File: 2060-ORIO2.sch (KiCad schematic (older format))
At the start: 197 parts, among them J11 RaspberryPI-B+header, J12 Conn_01x04, J13 Conn_01x08, J14 Conn_01x02, J15 Conn_01x08, J16 Conn_01x10, J17 Conn_01x10, J18 Conn_01x10, J19 Conn_01x10, J20 Conn_01x09, J21 Conn_01x08, J22 Conn_01x08, J23 Conn_01x08, J24 Conn_01x08, J25 Conn_01x08, J26 Conn_01x08, J28 Conn_01x16, J29 Conn_01x16, J30 Conn_01x16, J31 Conn_01x08, J32 Conn_01x08, J33 Conn_01x08, J34 Conn_01x08, J35 TBL001-500-02GY-2GY, Q11 ULN2803ADWR, Q12 BCV27, Q91 BCV27, Q92 BCV27, Q93 BCV27, Q94 BCV27, SW1 SW_DIP_x01, SW11 SW_DIP_x08, U1 AOZ2151TQI-19, U11 ICE40HX4K-TQ144, U12 ‎74LVT245B, U13 ‎74LVT245B, U14 ‎74LVT245B, U15 AOZ2151TQI-19, U16 MCP3008, U17 AZ1117CH-3.3TRG1, U18 AZ1117CH-3.3TRG1, U19 AZ1117CH-1.2, U20 AOZ2151TQI-19, U21 ‎74LVT245B, U22 ‎74LVT245B, U23 ‎74LVT245B, U24 ‎74LVT245B, U26 AP3012, Y11 XLH536025_000000I

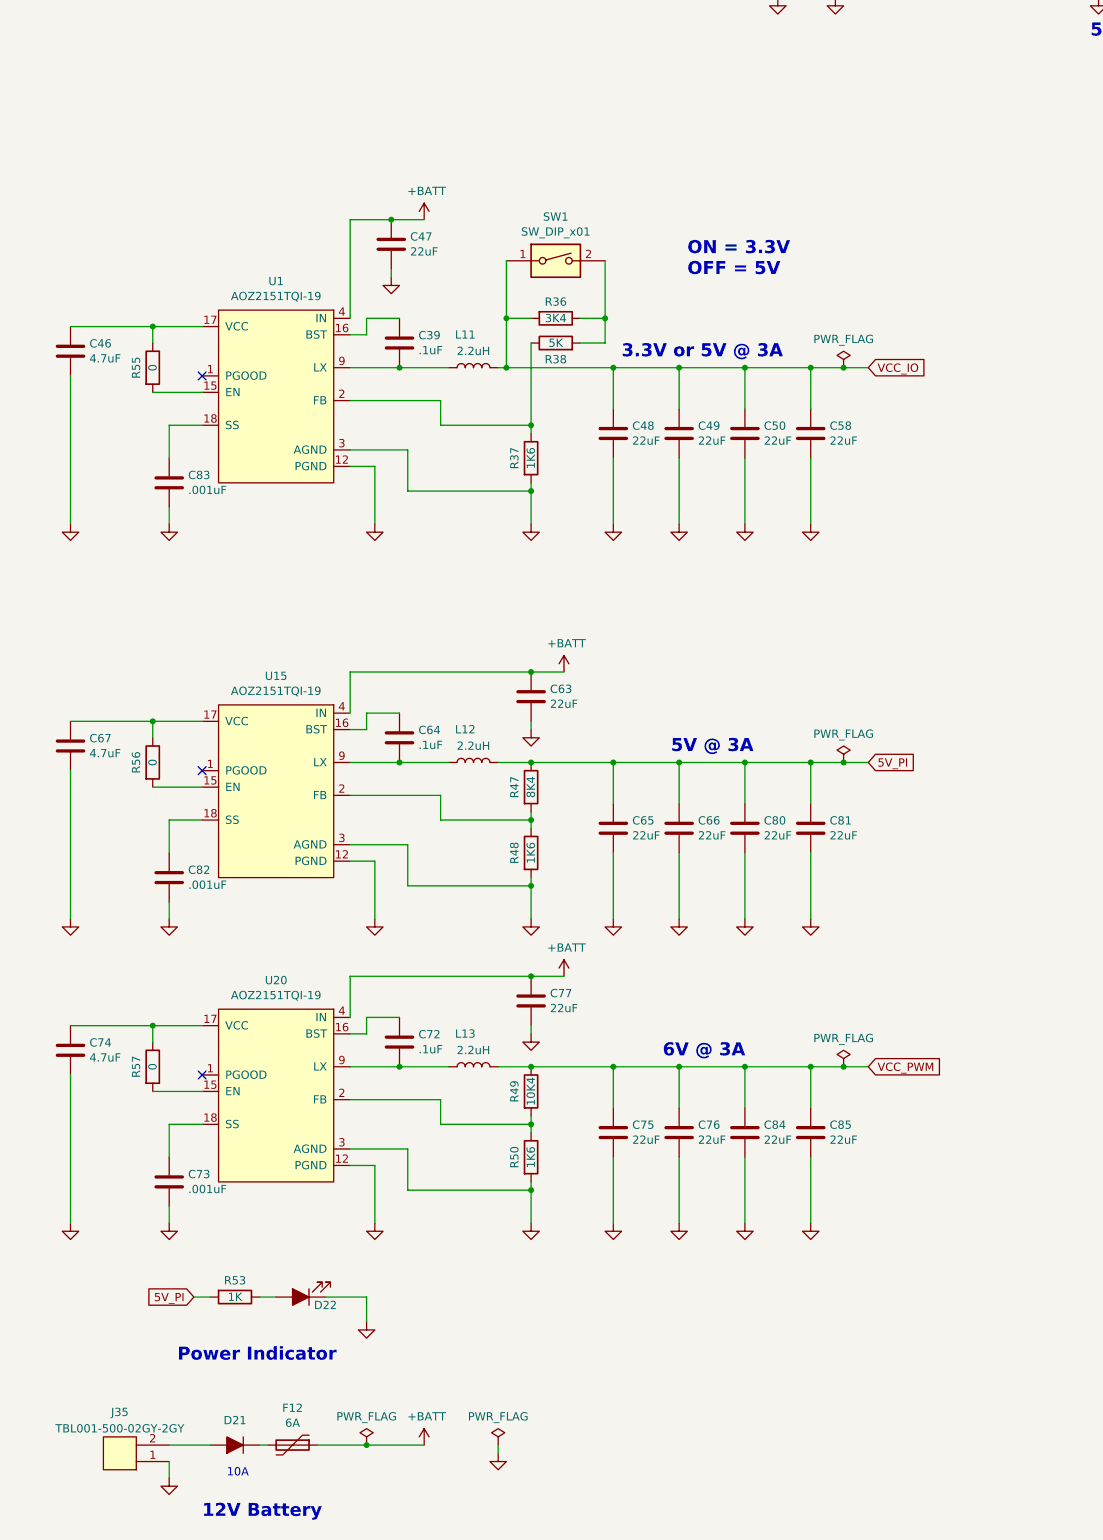
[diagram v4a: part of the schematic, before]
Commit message: Replace AOZ2151TQI-19 regulators with AP63300WU-7
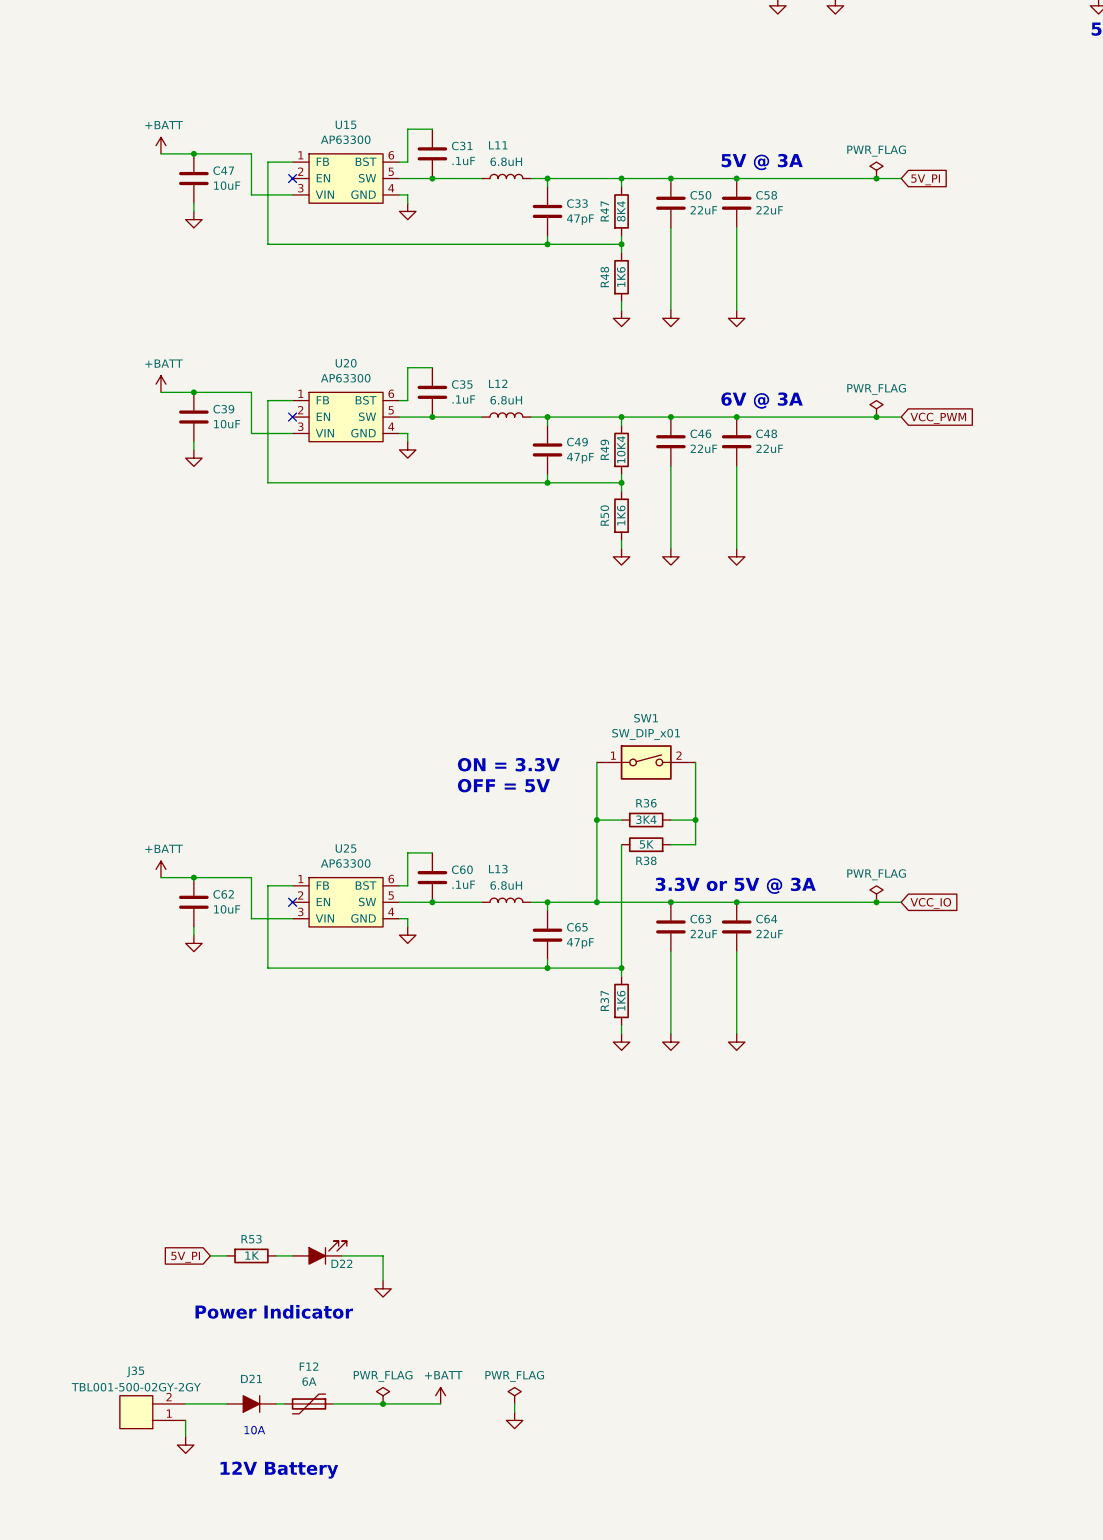
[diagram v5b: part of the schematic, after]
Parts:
- removed C66, C75, C76, C77, C80, C81, C84, C85: 22uF, Capacitor_SMD:C_0805_2012Metric_Pad1.15x1.40mm_HandSolder, symbol Device:C
- removed C67, C74: 4.7uF, Capacitor_SMD:C_0603_1608Metric_Pad1.05x0.95mm_HandSolder, symbol Device:C
- removed C72: .1uF, Capacitor_SMD:C_0603_1608Metric_Pad1.05x0.95mm_HandSolder, symbol Device:C
- removed C73, C82, C83: .001uF, Capacitor_SMD:C_0603_1608Metric_Pad1.05x0.95mm_HandSolder, symbol Device:C
- removed R55, R56, R57: 0, Resistor_SMD:R_0603_1608Metric_Pad1.05x0.95mm_HandSolder, symbol Device:R
- removed U1, U15, U20: AOZ2151TQI-19, jb-footprint:AOZ2151TQI-19, symbol jb-symbol:AOZ2151TQI-19
- added C31, C35, C60: .1uF, Capacitor_SMD:C_0603_1608Metric_Pad1.05x0.95mm_HandSolder, symbol Device:C
- added C33: 47pF, Capacitor_SMD:C_0603_1608Metric_Pad1.05x0.95mm_HandSolder, symbol Device:C
- added C62: 10uF, Capacitor_SMD:C_0805_2012Metric_Pad1.15x1.40mm_HandSolder, symbol Device:C
- added U15, U20, U25: AP63300, Package_TO_SOT_SMD:SOT-23-6, symbol jb-symbol:AP63300
- C39: value .1uF -> 10uF; footprint Capacitor_SMD:C_0603_1608Metric_Pad1.05x0.95mm_HandSolder -> Capacitor_SMD:C_0805_2012Metric_Pad1.15x1.40mm_HandSolder; Description CAP CER 0.1UF 25V X5R 0603 -> (none); Digi-Key_PN 445-6854-1-ND -> (none); MPN C1608X5R1E104K -> (none); Manufacturer TDK Corporation -> (none)
- C46: value 4.7uF -> 22uF; footprint Capacitor_SMD:C_0603_1608Metric_Pad1.05x0.95mm_HandSolder -> Capacitor_SMD:C_0805_2012Metric_Pad1.15x1.40mm_HandSolder; Description CAP CER 4.7UF 10V X5R 0603 -> CAP CER 22UF 10V X5R 0805; Digi-Key_PN 1276-1044-1-ND -> 490-10746-1-ND; MPN CL10A475KP8NNNC -> GRM21BR61A226ME44L; Manufacturer Samsung Electro-Mechanics -> Murata Electronics
- C47: value 22uF -> 10uF; Description CAP CER 22UF 25V X5R 0805 -> (none); Digi-Key_PN 490-14661-1-ND -> (none); MPN GRM21BR61E226ME44K -> (none); Manufacturer Murata Electronics -> (none)
- C49, C65: value 22uF -> 47pF; footprint Capacitor_SMD:C_0805_2012Metric_Pad1.15x1.40mm_HandSolder -> Capacitor_SMD:C_0603_1608Metric_Pad1.05x0.95mm_HandSolder; Description CAP CER 22UF 10V X5R 0805 -> (none); Digi-Key_PN 490-10746-1-ND -> (none); MPN GRM21BR61A226ME44L -> (none); Manufacturer Murata Electronics -> (none)
- C63: Description CAP CER 22UF 25V X5R 0805 -> CAP CER 22UF 10V X5R 0805; Digi-Key_PN 490-14661-1-ND -> 490-10746-1-ND; MPN GRM21BR61E226ME44K -> GRM21BR61A226ME44L
- C64: value .1uF -> 22uF; footprint Capacitor_SMD:C_0603_1608Metric_Pad1.05x0.95mm_HandSolder -> Capacitor_SMD:C_0805_2012Metric_Pad1.15x1.40mm_HandSolder; Description CAP CER 0.1UF 25V X5R 0603 -> CAP CER 22UF 10V X5R 0805; Digi-Key_PN 445-6854-1-ND -> 490-10746-1-ND; MPN C1608X5R1E104K -> GRM21BR61A226ME44L; Manufacturer TDK Corporation -> Murata Electronics
- L11, L12, L13: value 2.2uH -> 6.8uH; footprint Inductor_SMD:L_Taiyo-Yuden_MD-4040 -> Inductor_SMD:L_Bourns-SRN6028; Description FIXED IND 2.2UH 4.3A 48 MOHM SMD -> (none); Digi-Key_PN 553-3290-1-ND -> (none); MPN PA4332.222NLT -> (none); Manufacturer Pulse Electronics Power -> (none)
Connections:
- wire segments 1176 -> 1133
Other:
- moved on the sheet: C47, C50, C58, D21, D22, F12, J35, R37, R47, R48, R49, R50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

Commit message: Revision 2 as ordered from JLCPCB
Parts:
- removed Q91, Q92, Q93, Q94: BCV27, Package_TO_SOT_SMD:SOT-23, symbol Device:Q_NPN_Darlington_BEC
- added C66, C67, C69, C71, C72, C73: 22uF, Capacitor_SMD:C_0805_2012Metric_Pad1.15x1.40mm_HandSolder, symbol Device:C
- added J27: Conn_01x02, Connector_PinHeader_2.54mm:PinHeader_1x02_P2.54mm_Vertical, symbol Connector_Generic:Conn_01x02
- added Q13: BCV27, Package_TO_SOT_SMD:SOT-23, symbol Device:Q_NPN_Darlington_BEC
- added Q91, Q92, Q93, Q94: BCW65ALT1G, Package_TO_SOT_SMD:SOT-23, symbol Device:Q_NPN_BEC
- added R12: 1K, Resistor_SMD:R_0603_1608Metric_Pad1.05x0.95mm_HandSolder, symbol Device:R
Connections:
- net labels added: FPGA_AIR
- net labels removed: IOL_18B
- wire segments 1133 -> 1153
- no-connect marks 42 -> 41
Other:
- note added: "Compressor Relay\n(mount flyback diode on relay)"
- note added: "RS Light"
- note added: "closed = 3.3V\nopen = 5V"
- note removed: "ON = 3.3V\nOFF = 5V"
- note removed: "RSL Light Driver"
- moved on the sheet: C78, C79, D20, J14, L14, Q12, R51, R52, R54, R91, R92, R93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

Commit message: Move the PI connector, add filter caps, & tweak current limiter.
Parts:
- removed Q12, Q13: BCV27, Package_TO_SOT_SMD:SOT-23, symbol Device:Q_NPN_Darlington_BEC
- removed Q91, Q92, Q93, Q94: BCW65ALT1G, Package_TO_SOT_SMD:SOT-23, symbol Device:Q_NPN_BEC
- removed R91, R93: 10K, Resistor_SMD:R_0603_1608Metric_Pad1.05x0.95mm_HandSolder, symbol Device:R
- removed R92, R94: 1.2, Resistor_SMD:R_1210_3225Metric_Pad1.42x2.65mm_HandSolder, symbol Device:R
- added C74, C75, C76: 3300uF, Capacitor_THT:CP_Radial_D16.0mm_P7.50mm, symbol Device:CP1
- added C77: .1uF, Capacitor_SMD:C_0603_1608Metric_Pad1.08x0.95mm_HandSolder, symbol Device:C
- added D12: DB2460600L, Diode_SMD:D_SOD-128, symbol Device:D_Schottky_ALT
- added Q12, Q13: SSM3K376R, Package_TO_SOT_SMD:SOT-23, symbol Device:Q_NMOS_GSD
- added R13, R15: 1K, Resistor_SMD:R_0603_1608Metric_Pad0.98x0.95mm_HandSolder, symbol Device:R
- added RN15: 1K, Resistor_SMD:R_Array_Convex_8x0602, symbol Device:R_Pack08
- added U27: MC7812BDTG, Package_TO_SOT_SMD:TO-252-2, symbol Regulator_Linear:LM7812_TO220
- L11, L12, L13: Description (none) -> FIXED IND 6.8UH 3.6A 47 MOHM SMD; Digi-Key_PN (none) -> 445-173057-1-ND; MPN (none) -> VLS6045EX-6R8M; Manufacturer (none) -> TDK Corporation
- R12, R54: value 1K -> 100; footprint Resistor_SMD:R_0603_1608Metric_Pad1.05x0.95mm_HandSolder -> Resistor_SMD:R_0603_1608Metric_Pad0.98x0.95mm_HandSolder; Description RES SMD 1K OHM 1% 1/10W 0603 -> RES SMD 100 OHM 1% 1/10W 0603; Digi-Key_PN 311-1.00KHRCT-ND -> 311-100HRCT-ND; MPN RC0603FR-071KL -> RC0603FR-07100RL
- RN14: Digi-Key_PN (none) -> Y1330CT-ND; MPN (none) -> EXB-2HV330JV
- U15, U20, U25: Description (none) -> DCDC CONV HV 3A BUCK TSOT26; Digi-Key_PN (none) -> 31-AP63300WU-7CT-ND; MPN (none) -> AP63300WU-7; Manufacturer (none) -> Diodes Incorporated
- renumbered D12 to D0, D13 to D1, D14 to D2, D15 to D3, D16 to D4, D17 to D5, D18 to D6, D19 to D7
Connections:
- net labels added: VB_LIM
- net labels removed: VB_RSL, VB_RSOL
- wire segments 1153 -> 1167
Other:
- note added: "Compressor Relay"
- note added: "Current Limiter"
- note removed: ".5 Watt"
- note removed: "500ma Current Limiter"
- note removed: "Compressor Relay\n(mount flyback diode on relay)"
- moved on the sheet: D0, D1, D2, D3, D4, D5, D6, D7, J12, R23, R24, RN11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

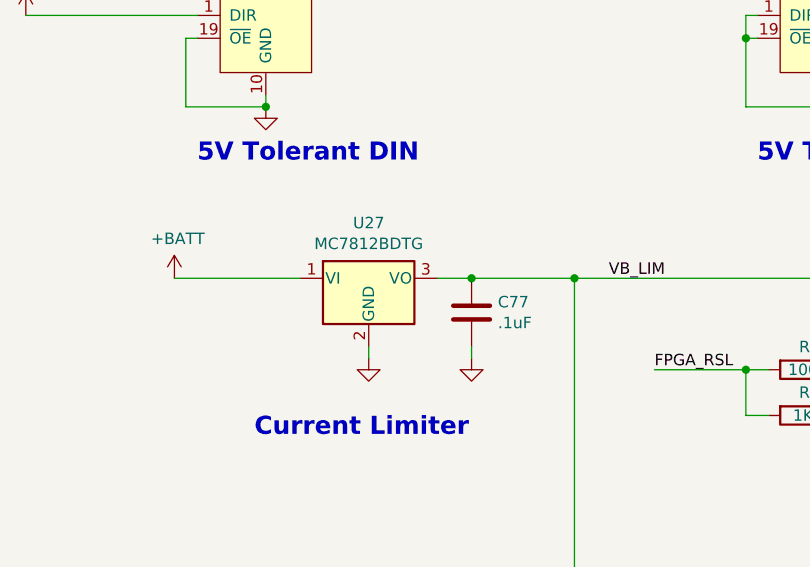
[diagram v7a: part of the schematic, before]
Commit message: Change 12V LDO, header & cap clearance
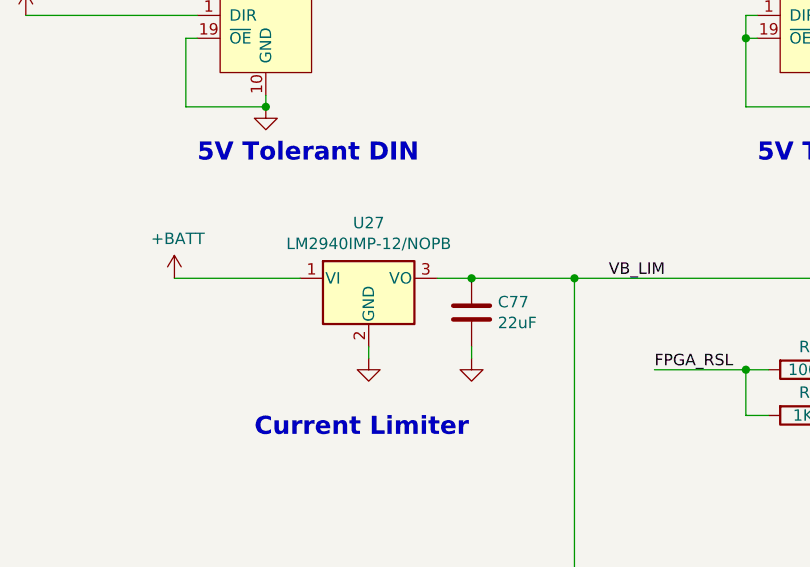
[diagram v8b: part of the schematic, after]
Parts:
- C77: value .1uF -> 22uF; footprint Capacitor_SMD:C_0603_1608Metric_Pad1.08x0.95mm_HandSolder -> Capacitor_SMD:C_0805_2012Metric_Pad1.15x1.40mm_HandSolder; Description CAP CER 0.1UF 25V X5R 0603 -> 22UF 25V X5R; Digi-Key_PN 445-6854-1-ND -> 490-14661-1-ND; MPN C1608X5R1E104K -> (none); Manufacturer TDK Corporation -> (none)
- U27: value MC7812BDTG -> LM2940IMP-12/NOPB; footprint Package_TO_SOT_SMD:TO-252-2 -> Package_TO_SOT_SMD:TO-252-3_TabPin2; Description IC REG LINEAR 12V 1A DPAK -> Linear Voltage Regulator IC 1 Output 1A SOT-223-4; Digi-Key_PN MC7812BDTGOS-ND -> LM2940IMP-12/NOPBCT-ND; MPN MC7812BDTG -> LM2940IMP-12/NOPB; Manufacturer ON Semiconductor -> Texas Instruments
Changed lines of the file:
@@
 P 10250 12800
 F 0 "U27" H 10250 13042 50  0000 C CNN
-F 1 "MC7812BDTG" H 10250 12951 50  0000 C CNN
-F 2 "Package_TO_SOT_SMD:TO-252-2" H 10250 13025 50  0001 C CIN
+F 1 "LM2940IMP-12/NOPB" H 10250 12951 50  0000 C CNN
+F 2 "Package_TO_SOT_SMD:TO-252-3_TabPin2" H 10250 13025 50  0001 C CIN
 F 3 "" H 10250 12750 50  0001 C CNN
-F 4 "IC REG LINEAR 12V 1A DPAK" H 10250 12800 50  0001 C CNN "Description"
-F 5 "MC7812BDTGOS-ND" H 10250 12800 50  0001 C CNN "Digi-Key_PN"
-F 6 "MC7812BDTG" H 10250 12800 50  0001 C CNN "MPN"
-F 7 "ON Semiconductor" H 10250 12800 50  0001 C CNN "Manufacturer"
+F 4 "Linear Voltage Regulator IC  1 Output  1A SOT-223-4" H 10250 12800 50  0001 C CNN "Description"
+F 5 "LM2940IMP-12/NOPBCT-ND" H 10250 12800 50  0001 C CNN "Digi-Key_PN"
+F 6 "LM2940IMP-12/NOPB" H 10250 12800 50  0001 C CNN "MPN"
+F 7 "Texas Instruments" H 10250 12800 50  0001 C CNN "Manufacturer"
 	1    10250 12800
 	1    0    0    -1
@@
 $EndComp
 Connection ~ 11150 12800
-Wire Wire Line
-	10550 12800 10700 12800
 Wire Wire Line
 	11150 12800 13150 12800
@@
 $EndComp
 $Comp
-L Device:C C?
-U 1 1 60B02461
-P 10700 12950
-AR Path="/5F66828B/60B02461" Ref="C?"  Part="1"
-AR Path="/60B02461" Ref="C77"  Part="1"
-F 0 "C77" H 10815 12996 50  0000 L CNN
-F 1 ".1uF" H 10815 12905 50  0000 L CNN
-F 2 "Capacitor_SMD:C_0603_1608Metric_Pad1.08x0.95mm_HandSolder" H 10738 12800 50  0001 C CNN
-F 3 "~" H 10700 12950 50  0001 C CNN
-F 4 "CAP CER 0.1UF 25V X5R 0603" H 10700 12950 50  0001 C CNN "Description"
-F 5 "445-6854-1-ND" H 10700 12950 50  0001 C CNN "Digi-Key_PN"
-F 6 "C1608X5R1E104K" H 10700 12950 50  0001 C CNN "MPN"
-F 7 "TDK Corporation" H 10700 12950 50  0001 C CNN "Manufacturer"
-	1    10700 12950
-	1    0    0    -1
-$EndComp
-Connection ~ 10700 12800
-Wire Wire Line
-	10700 12800 11150 12800
-$Comp
 L power:GND #PWR094
 U 1 1 60CB4A83
@@
 	12750 13850 12750 13950
 Connection ~ 12750 13950
+$Comp
+L Device:C C?
+U 1 1 601BE493
+P 10700 12950
+AR Path="/5BBE5CCD/601BE493" Ref="C?"  Part="1"
+AR Path="/601BE493" Ref="C77"  Part="1"
+AR Path="/5CF9559A/601BE493" Ref="C?"  Part="1"
+AR Path="/5DFE66B1/601BE493" Ref="C?"  Part="1"
+AR Path="/5ECC13DB/5DFE66B1/601BE493" Ref="C?"  Part="1"
+AR Path="/5F51430C/601BE493" Ref="C?"  Part="1"
+F 0 "C77" H 10815 12996 50  0000 L CNN
+F 1 "22uF" H 10815 12905 50  0000 L CNN
+F 2 "Capacitor_SMD:C_0805_2012Metric_Pad1.15x1.40mm_HandSolder" H 10738 12800 50  0001 C CNN
+F 3 "~" H 10700 12950 50  0001 C CNN
+F 4 "490-14661-1-ND" H 11100 12700 50  0001 C CNN "Digi-Key_PN"
+F 5 "22UF 25V X5R" H 10700 12950 50  0001 C CNN "Description"
+F 6 "" H 10700 12950 50  0001 C CNN "MPN"
+F 7 "" H 10700 12950 50  0001 C CNN "Manufacturer"
+	1    10700 12950
+	1    0    0    -1
+$EndComp
+Wire Wire Line
+	10550 12800 10700 12800
+Connection ~ 10700 12800
+Wire Wire Line
+	10700 12800 11150 12800
 $EndSCHEMATC
